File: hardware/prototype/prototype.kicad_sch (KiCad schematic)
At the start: 5 parts, among them Q1 2N2222A, U2 RP2040-ZERO

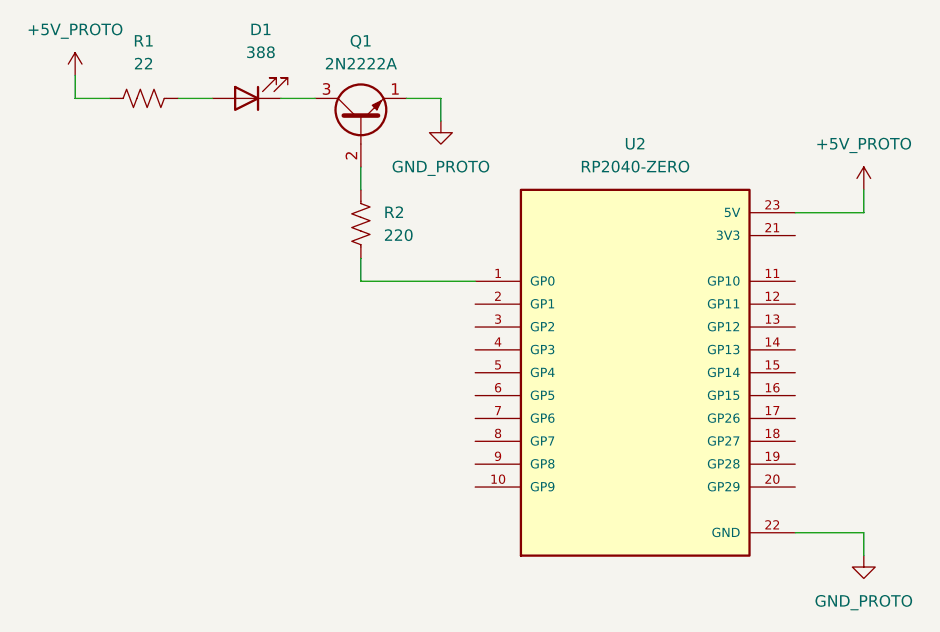
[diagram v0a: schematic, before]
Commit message: started placing leds
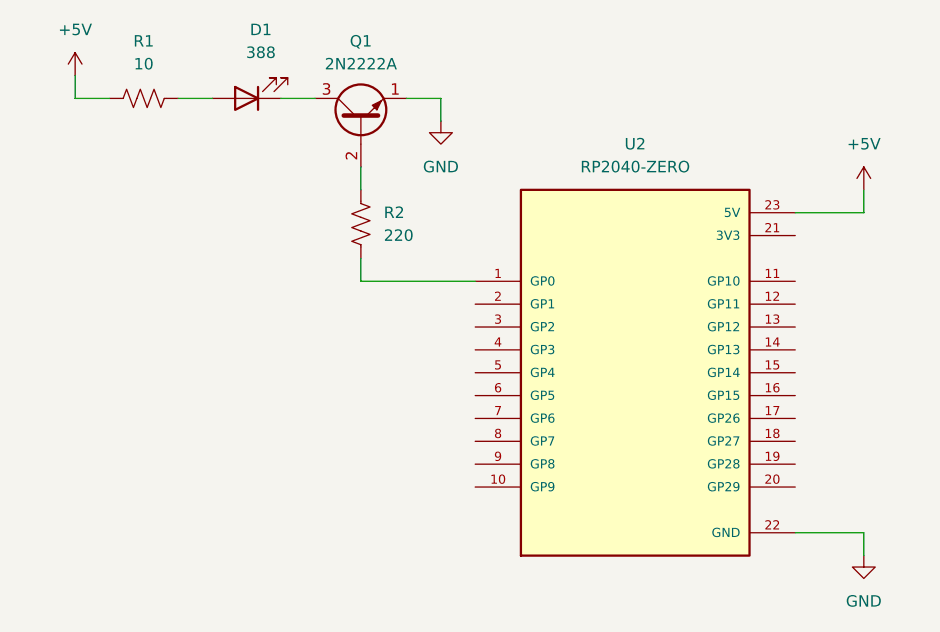
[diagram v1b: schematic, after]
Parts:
- R1: value 22 -> 10
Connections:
- net +5V_PROTO renamed +5V
- net GND_PROTO renamed GND
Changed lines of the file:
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@@
-	)
-	(symbol
-		(lib_id "power:GND")
-		(at 129.54 73.66 0)
-		(unit 1)
-		(body_style 1)
-		(exclude_from_sim no)
-		(in_bom yes)
-		(on_board yes)
-		(in_pos_files yes)
-		(dnp no)
-		(fields_autoplaced yes)
-		(property "Reference" "#PWR013"
-			(at 129.54 80.01 0)
-			(hide yes)
-			(show_name no)
-			(do_not_autoplace no)
-			(effects
-				(font
-					(size 1.27 1.27)
-				)
-			)
-		)
-		(property "Value" "GND_PROTO"
-			(at 129.54 78.74 0)
-			(show_name no)
-			(do_not_autoplace no)
-			(effects
-				(font
-					(size 1.27 1.27)
-				)
-			)
-		)
-		(property "Footprint" ""
-			(at 129.54 73.66 0)
-			(hide yes)
-			(show_name no)
-			(do_not_autoplace no)
-			(effects
-				(font
-					(size 1.27 1.27)
-				)
-			)
-		)
-		(property "Datasheet" ""
-			(at 129.54 73.66 0)
-			(hide yes)
-			(show_name no)
-			(do_not_autoplace no)
-			(effects
-				(font
-					(size 1.27 1.27)
-				)
-			)
-		)
-		(property "Description" "Power symbol creates a global label with name \"GND\" , ground"
-			(at 129.54 73.66 0)
-			(hide yes)
-			(show_name no)
-			(do_not_autoplace no)
-			(effects
-				(font
-					(size 1.27 1.27)
-				)
-			)
-		)
-		(pin "1"
-		)
-		(instances
-			(project "LBD"
-				(path "/79b525c5-f9c9-456f-9ae1-5cb9eb4f2523"
-					(reference "#PWR013")
-					(unit 1)
-				)
-			)
-			(project "prototype"
-				(path "/8816677f-95c4-480c-93bb-e367c3bc16fa"
-					(reference "#PWR013")
-					(unit 1)
-				)
-			)
-		)
 	)
 	(symbol
@@
 			)
 		)
-		(property "Value" "22"
+		(property "Value" "10"
 			(at 96.52 67.31 90)
 			(show_name no)
@@
 	)
 	(symbol
-		(lib_id "power:+5V")
-		(at 176.53 81.28 0)
+		(lib_id "power:GND")
+		(at 129.54 73.66 0)
 		(unit 1)
 		(body_style 1)
@@
 		(dnp no)
 		(fields_autoplaced yes)
-		(property "Reference" "#PWR05"
-			(at 176.53 85.09 0)
-			(hide yes)
-			(show_name no)
-			(do_not_autoplace no)
-			(effects
-				(font
-					(size 1.27 1.27)
-				)
-			)
-		)
-		(property "Value" "+5V_PROTO"
-			(at 176.53 76.2 0)
+		(property "Reference" "#PWR04"
+			(at 129.54 80.01 0)
+			(hide yes)
+			(show_name no)
+			(do_not_autoplace no)
+			(effects
+				(font
+					(size 1.27 1.27)
+				)
+			)
+		)
+		(property "Value" "GND"
+			(at 129.54 78.74 0)
 			(show_name no)
 			(do_not_autoplace no)
@@
 		)
 		(property "Footprint" ""
-			(at 176.53 81.28 0)
+			(at 129.54 73.66 0)
 			(hide yes)
 			(show_name no)
@@
 		)
 		(property "Datasheet" ""
-			(at 176.53 81.28 0)
-			(hide yes)
-			(show_name no)
-			(do_not_autoplace no)
-			(effects
-				(font
-					(size 1.27 1.27)
-				)
-			)
-		)
-		(property "Description" "Power symbol creates a global label with name \"+5V\""
-			(at 176.53 81.28 0)
+			(at 129.54 73.66 0)
+			(hide yes)
+			(show_name no)
+			(do_not_autoplace no)
+			(effects
+				(font
+					(size 1.27 1.27)
+				)
+			)
+		)
+		(property "Description" "Power symbol creates a global label with name \"GND\" , ground"
+			(at 129.54 73.66 0)
 			(hide yes)
 			(show_name no)
@@
 		)
 		(instances
-			(project "LBD"
-				(path "/79b525c5-f9c9-456f-9ae1-5cb9eb4f2523"
-					(reference "#PWR05")
-					(unit 1)
-				)
-			)
 			(project "prototype"
 				(path "/8816677f-95c4-480c-93bb-e367c3bc16fa"
-					(reference "#PWR05")
+					(reference "#PWR04")
 					(unit 1)
 				)
@@
 	)
 	(symbol
-		(lib_id "power:+5V")
-		(at 88.9 68.58 0)
-		(unit 1)
-		(body_style 1)
-		(exclude_from_sim no)
-		(in_bom yes)
-		(on_board yes)
-		(in_pos_files yes)
-		(dnp no)
-		(fields_autoplaced yes)
-		(property "Reference" "#PWR012"
-			(at 88.9 72.39 0)
-			(hide yes)
-			(show_name no)
-			(do_not_autoplace no)
-			(effects
-				(font
-					(size 1.27 1.27)
-				)
-			)
-		)
-		(property "Value" "+5V_PROTO"
-			(at 88.9 63.5 0)
-			(show_name no)
-			(do_not_autoplace no)
-			(effects
-				(font
-					(size 1.27 1.27)
-				)
-			)
-		)
-		(property "Footprint" ""
-			(at 88.9 68.58 0)
-			(hide yes)
-			(show_name no)
-			(do_not_autoplace no)
-			(effects
-				(font
-					(size 1.27 1.27)
-				)
-			)
-		)
-		(property "Datasheet" ""
-			(at 88.9 68.58 0)
-			(hide yes)
-			(show_name no)
-			(do_not_autoplace no)
-			(effects
-				(font
-					(size 1.27 1.27)
-				)
-			)
-		)
-		(property "Description" "Power symbol creates a global label with name \"+5V\""
-			(at 88.9 68.58 0)
-			(hide yes)
-			(show_name no)
-			(do_not_autoplace no)
-			(effects
-				(font
-					(size 1.27 1.27)
-				)
-			)
-		)
-		(pin "1"
-		)
-		(instances
-			(project "LBD"
-				(path "/79b525c5-f9c9-456f-9ae1-5cb9eb4f2523"
-					(reference "#PWR012")
-					(unit 1)
-				)
-			)
-			(project "prototype"
-				(path "/8816677f-95c4-480c-93bb-e367c3bc16fa"
-					(reference "#PWR012")
-					(unit 1)
-				)
-			)
-		)
-	)
-	(symbol
 		(lib_id "Transistor_BJT:Q_NPN_EBC")
 		(at 120.65 73.66 90)
@@
 		(dnp no)
 		(fields_autoplaced yes)
-		(property "Reference" "#PWR06"
+		(property "Reference" "#PWR03"
 			(at 176.53 128.27 0)
 			(hide yes)
@@
 			)
 		)
-		(property "Value" "GND_PROTO"
+		(property "Value" "GND"
 			(at 176.53 127 0)
 			(show_name no)
@@
 		)
 		(instances
-			(project "LBD"
-				(path "/79b525c5-f9c9-456f-9ae1-5cb9eb4f2523"
-					(reference "#PWR06")
-					(unit 1)
-				)
-			)
 			(project "prototype"
 				(path "/8816677f-95c4-480c-93bb-e367c3bc16fa"
-					(reference "#PWR06")
+					(reference "#PWR03")
 					(unit 1)
 				)
@@
 	)
 	(symbol
+		(lib_id "power:+5V")
+		(at 176.53 81.28 0)
+		(unit 1)
+		(body_style 1)
+		(exclude_from_sim no)
+		(in_bom yes)
+		(on_board yes)
+		(in_pos_files yes)
+		(dnp no)
+		(fields_autoplaced yes)
+		(property "Reference" "#PWR02"
+			(at 176.53 85.09 0)
+			(hide yes)
+			(show_name no)
+			(do_not_autoplace no)
+			(effects
+				(font
+					(size 1.27 1.27)
+				)
+			)
+		)
+		(property "Value" "+5V"
+			(at 176.53 76.2 0)
+			(show_name no)
+			(do_not_autoplace no)
+			(effects
+				(font
+					(size 1.27 1.27)
+				)
+			)
+		)
+		(property "Footprint" ""
+			(at 176.53 81.28 0)
+			(hide yes)
+			(show_name no)
+			(do_not_autoplace no)
+			(effects
+				(font
+					(size 1.27 1.27)
+				)
+			)
+		)
+		(property "Datasheet" ""
+			(at 176.53 81.28 0)
+			(hide yes)
+			(show_name no)
+			(do_not_autoplace no)
+			(effects
+				(font
+					(size 1.27 1.27)
+				)
+			)
+		)
+		(property "Description" "Power symbol creates a global label with name \"+5V\""
+			(at 176.53 81.28 0)
+			(hide yes)
+			(show_name no)
+			(do_not_autoplace no)
+			(effects
+				(font
+					(size 1.27 1.27)
+				)
+			)
+		)
+		(pin "1"
+		)
+		(instances
+			(project "prototype"
+				(path "/8816677f-95c4-480c-93bb-e367c3bc16fa"
+					(reference "#PWR02")
+					(unit 1)
+				)
+			)
+		)
+	)
+	(symbol
+		(lib_id "power:+5V")
+		(at 88.9 68.58 0)
+		(unit 1)
+		(body_style 1)
+		(exclude_from_sim no)
+		(in_bom yes)
+		(on_board yes)
+		(in_pos_files yes)
+		(dnp no)
+		(fields_autoplaced yes)
+		(property "Reference" "#PWR01"
+			(at 88.9 72.39 0)
+			(hide yes)
+			(show_name no)
+			(do_not_autoplace no)
+			(effects
+				(font
+					(size 1.27 1.27)
+				)
+			)
+		)
+		(property "Value" "+5V"
+			(at 88.9 63.5 0)
+			(show_name no)
+			(do_not_autoplace no)
+			(effects
+				(font
+					(size 1.27 1.27)
+				)
+			)
+		)
+		(property "Footprint" ""
+			(at 88.9 68.58 0)
+			(hide yes)
+			(show_name no)
+			(do_not_autoplace no)
+			(effects
+				(font
+					(size 1.27 1.27)
+				)
+			)
+		)
+		(property "Datasheet" ""
+			(at 88.9 68.58 0)
+			(hide yes)
+			(show_name no)
+			(do_not_autoplace no)
+			(effects
+				(font
+					(size 1.27 1.27)
+				)
+			)
+		)
+		(property "Description" "Power symbol creates a global label with name \"+5V\""
+			(at 88.9 68.58 0)
+			(hide yes)
+			(show_name no)
+			(do_not_autoplace no)
+			(effects
+				(font
+					(size 1.27 1.27)
+				)
+			)
+		)
+		(pin "1"
+		)
+		(instances
+			(project "prototype"
+				(path "/8816677f-95c4-480c-93bb-e367c3bc16fa"
+					(reference "#PWR01")
+					(unit 1)
+				)
+			)
+		)
+	)
+	(symbol
 		(lib_id "Device:R_US")
 		(at 120.65 85.09 0)
@@
 	(sheet_instances
 		(path "/"
-			(page "5")
-		)
-	)
+			(page "1")
+		)
+	)
